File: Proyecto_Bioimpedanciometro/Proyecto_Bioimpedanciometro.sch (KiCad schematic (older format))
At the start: 29 parts, among them IC1 ATMEGA328P-A, P1 CONN_01X10, P2 CONN_01X04, U1 ADG849, U2 AD8606, U3 APD3339, Y1 Crystal_Small

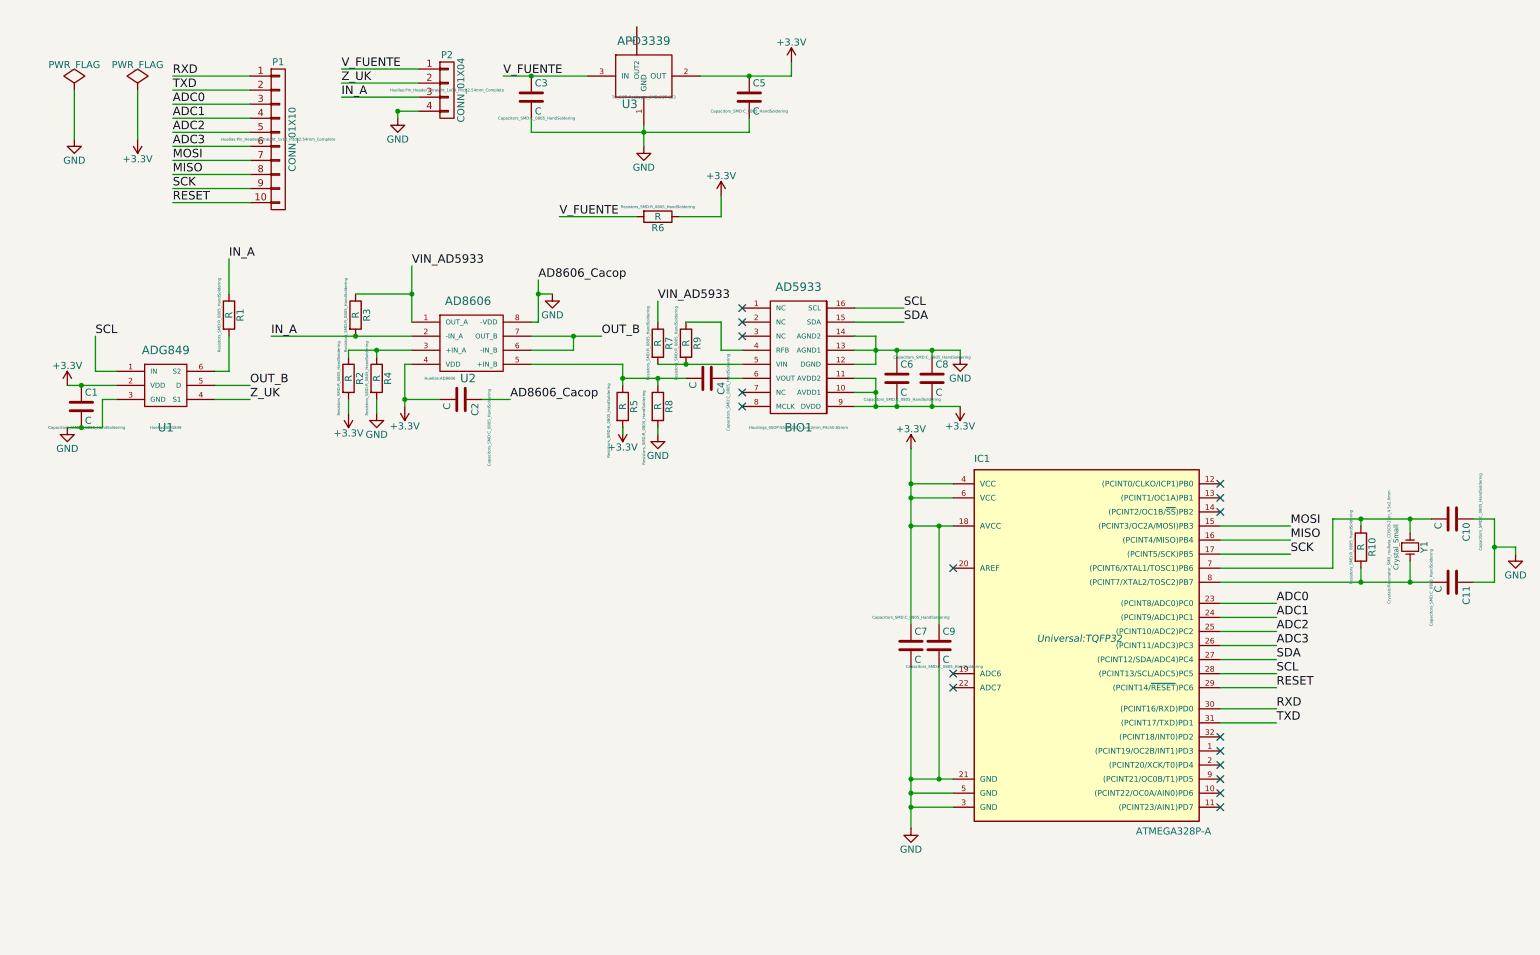
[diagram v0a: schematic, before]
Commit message: Segunda Version
Empieza PCB
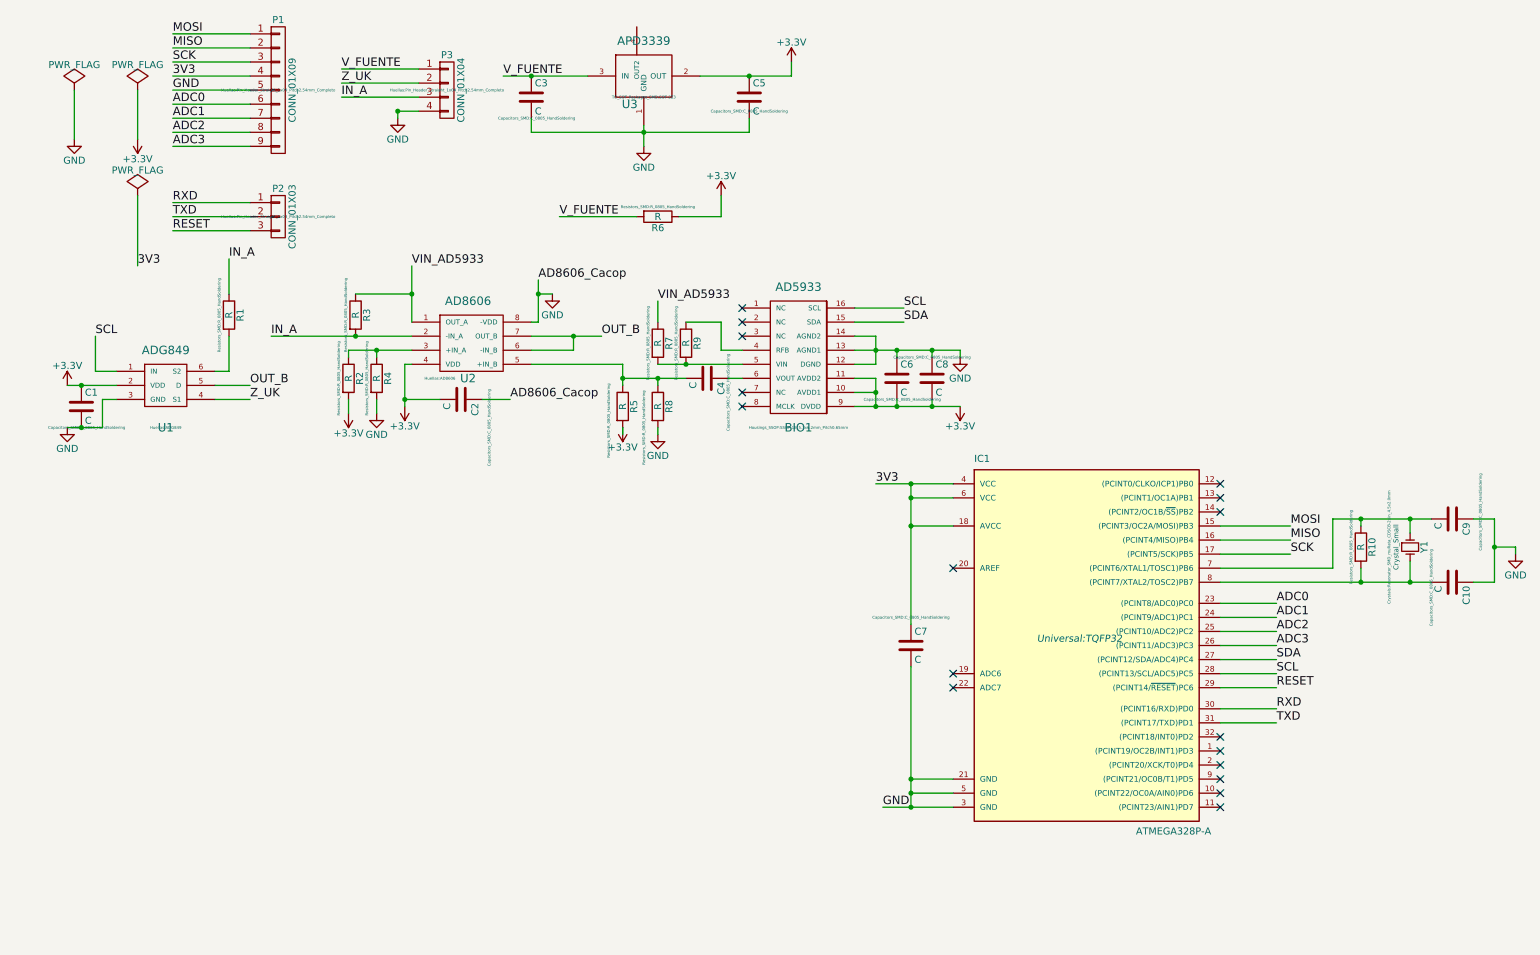
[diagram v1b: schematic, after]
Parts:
- removed C9: C, Capacitors_SMD:C_0805_HandSoldering, symbol C
- removed P1: CONN_01X10, Huellas:Pin_Header_Straight_1x10_Pitch2.54mm_Completo, symbol CONN_01X10
- added P1: CONN_01X09, Huellas:Pin_Header_Straight_1x09_Pitch2.54mm_Completo, symbol CONN_01X09
- added P2: CONN_01X03, Huellas:Pin_Header_Straight_1x03_Pitch2.54mm_Completo, symbol CONN_01X03
- renumbered C11 to C10, C10 to C9, P2 to P3
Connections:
- net +3V3: no longer C7.1, IC1.18 (AVCC), IC1.4 (VCC), IC1.6 (VCC)
- net ADC0: now also P1.6 (P6)
- net ADC1: now also P1.7 (P7)
- net ADC2: now also P1.8 (P8)
- net ADC3: now also P1.9 (P9)
- net GND: now also P1.5 (P5)
- net MISO: now also P1.2 (P2)
- net MOSI: now also P1.1 (P1)
- net RESET: now also P2.3 (P3)
- net RXD: now also P2.1 (P1)
- net SCK: now also P1.3 (P3)
- net TXD: now also P2.2 (P2)
- new net 3V3: C7.1, IC1.18 (AVCC), IC1.4 (VCC), IC1.6 (VCC), P1.4 (P4)
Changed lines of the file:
@@
 	-1   0    0    1
-$EndComp
-$Comp
-L +3.3V #PWR09
-U 1 1 5906C3D4
-P 6850 3600
-F 0 "#PWR09" H 6850 3450 50  0001 C CNN
-F 1 "+3.3V" H 6850 3740 50  0000 C CNN
-F 2 "" H 6850 3600 50  0000 C CNN
-F 3 "" H 6850 3600 50  0000 C CNN
-	1    6850 3600
-	1    0    0    -1
-$EndComp
-$Comp
-L GND #PWR010
-U 1 1 5906C412
-P 6850 6300
-F 0 "#PWR010" H 6850 6050 50  0001 C CNN
-F 1 "GND" H 6850 6150 50  0000 C CNN
-F 2 "" H 6850 6300 50  0000 C CNN
-F 3 "" H 6850 6300 50  0000 C CNN
-	1    6850 6300
-	1    0    0    -1
 $EndComp
 Text Label 2150 3150 0    60   ~ 0
@@
 NoConn ~ 7150 4450
 $Comp
-L GND #PWR011
+L GND #PWR09
 U 1 1 5908C4BA
 P 4950 1450
-F 0 "#PWR011" H 4950 1200 50  0001 C CNN
+F 0 "#PWR09" H 4950 1200 50  0001 C CNN
 F 1 "GND" H 4950 1300 50  0000 C CNN
 F 2 "" H 4950 1450 50  0000 C CNN
@@
 $EndComp
 $Comp
-L +3.3V #PWR012
+L +3.3V #PWR010
 U 1 1 5908C540
 P 6000 850
-F 0 "#PWR012" H 6000 700 50  0001 C CNN
+F 0 "#PWR010" H 6000 700 50  0001 C CNN
 F 1 "+3.3V" H 6000 990 50  0000 C CNN
 F 2 "" H 6000 850 50  0000 C CNN
@@
 $EndComp
 $Comp
-L GND #PWR013
+L GND #PWR011
 U 1 1 59090FFD
 P 4300 2500
-F 0 "#PWR013" H 4300 2250 50  0001 C CNN
+F 0 "#PWR011" H 4300 2250 50  0001 C CNN
 F 1 "GND" H 4300 2350 50  0000 C CNN
 F 2 "" H 4300 2500 50  0000 C CNN
@@
 $EndComp
 $Comp
-L +3.3V #PWR014
+L +3.3V #PWR012
 U 1 1 5909102D
 P 3250 3300
-F 0 "#PWR014" H 3250 3150 50  0001 C CNN
+F 0 "#PWR012" H 3250 3150 50  0001 C CNN
 F 1 "+3.3V" H 3250 3440 50  0000 C CNN
 F 2 "" H 3250 3300 50  0000 C CNN
@@
 Z_UK
 $Comp
-L GND #PWR015
+L GND #PWR013
 U 1 1 590947E6
 P 3200 1250
-F 0 "#PWR015" H 3200 1000 50  0001 C CNN
+F 0 "#PWR013" H 3200 1000 50  0001 C CNN
 F 1 "GND" H 3200 1100 50  0000 C CNN
 F 2 "" H 3200 1250 50  0000 C CNN
@@
 $EndComp
 $Comp
-L +3.3V #PWR016
+L +3.3V #PWR014
 U 1 1 5909785B
 P 5500 1800
-F 0 "#PWR016" H 5500 1650 50  0001 C CNN
+F 0 "#PWR014" H 5500 1650 50  0001 C CNN
 F 1 "+3.3V" H 5500 1940 50  0000 C CNN
 F 2 "" H 5500 1800 50  0000 C CNN
@@
 IN_A
 $Comp
-L PWR_FLAG #FLG017
+L PWR_FLAG #FLG015
 U 1 1 590A29EE
 P 900 1050
-F 0 "#FLG017" H 900 1145 50  0001 C CNN
+F 0 "#FLG015" H 900 1145 50  0001 C CNN
 F 1 "PWR_FLAG" H 900 1230 50  0000 C CNN
 F 2 "" H 900 1050 50  0000 C CNN
@@
 $EndComp
 $Comp
-L PWR_FLAG #FLG018
+L PWR_FLAG #FLG016
 U 1 1 590A2A28
 P 1350 1050
-F 0 "#FLG018" H 1350 1145 50  0001 C CNN
+F 0 "#FLG016" H 1350 1145 50  0001 C CNN
 F 1 "PWR_FLAG" H 1350 1230 50  0000 C CNN
 F 2 "" H 1350 1050 50  0000 C CNN
@@
 $EndComp
 $Comp
-L GND #PWR019
+L GND #PWR017
 U 1 1 590A2B52
 P 900 1400
-F 0 "#PWR019" H 900 1150 50  0001 C CNN
+F 0 "#PWR017" H 900 1150 50  0001 C CNN
 F 1 "GND" H 900 1250 50  0000 C CNN
 F 2 "" H 900 1400 50  0000 C CNN
@@
 $EndComp
 $Comp
-L +3.3V #PWR020
+L +3.3V #PWR018
 U 1 1 590A2B8C
 P 1350 1400
-F 0 "#PWR020" H 1350 1250 50  0001 C CNN
+F 0 "#PWR018" H 1350 1250 50  0001 C CNN
 F 1 "+3.3V" H 1350 1540 50  0000 C CNN
 F 2 "" H 1350 1400 50  0000 C CNN
@@
 $EndComp
 $Comp
-L C C10
+L C C9
 U 1 1 590BC56B
 P 10700 4100
-F 0 "C10" H 10725 4200 50  0000 L CNN
+F 0 "C9" H 10725 4200 50  0000 L CNN
 F 1 "C" H 10725 4000 50  0000 L CNN
 F 2 "Capacitors_SMD:C_0805_HandSoldering" H 10650 4300 20  0000 C CNN
@@
 $EndComp
 $Comp
-L C C11
+L C C10
 U 1 1 590BC5EC
 P 10700 4550
-F 0 "C11" H 10725 4650 50  0000 L CNN
+F 0 "C10" H 10725 4650 50  0000 L CNN
 F 1 "C" H 10725 4450 50  0000 L CNN
 F 2 "Capacitors_SMD:C_0805_HandSoldering" H 10738 4400 20  0000 C CNN
@@
 $EndComp
 $Comp
-L GND #PWR021
+L GND #PWR019
 U 1 1 590BD420
 P 11150 4350
-F 0 "#PWR021" H 11150 4100 50  0001 C CNN
+F 0 "#PWR019" H 11150 4100 50  0001 C CNN
 F 1 "GND" H 11150 4200 50  0000 C CNN
 F 2 "" H 11150 4350 50  0000 C CNN
@@
 	1    0    0    -1
 $EndComp
-$Comp
-L C C9
-U 1 1 590CC03D
-P 7050 5000
-F 0 "C9" H 7075 5100 50  0000 L CNN
-F 1 "C" H 7075 4900 50  0000 L CNN
-F 2 "Capacitors_SMD:C_0805_HandSoldering" H 7088 4850 20  0000 C CNN
-F 3 "" H 7050 5000 50  0000 C CNN
-	1    7050 5000
-	1    0    0    -1
-$EndComp
 Wire Wire Line
 	4800 3000 4800 3150
@@
 	9050 5200 9450 5200
 Wire Wire Line
-	6850 3600 6850 4850
-Wire Wire Line
-	6850 4150 7150 4150
-Connection ~ 6850 3850
-Wire Wire Line
-	6850 6150 7150 6150
-Wire Wire Line
-	6850 5150 6850 6300
+	6650 6150 7150 6150
 Wire Wire Line
 	6850 6050 7150 6050
@@
 	9050 4700 9450 4700
 Wire Wire Line
+	2150 850  1600 850
+Wire Wire Line
 	2150 1150 1600 1150
 Wire Wire Line
@@
 Wire Wire Line
 	2150 1350 1600 1350
-Wire Wire Line
-	2150 1450 1600 1450
 Wire Wire Line
 	9050 4550 10550 4550
@@
 	11150 4300 11150 4350
 Connection ~ 11000 4300
-Connection ~ 6850 3950
 Wire Wire Line
 	6850 5950 7150 5950
@@
 	7000 2950 7000 2900
 Connection ~ 7000 2900
-Wire Wire Line
-	7150 3950 6850 3950
-Wire Wire Line
-	7150 3850 6850 3850
 Connection ~ 6850 6050
-Connection ~ 6850 6150
-Connection ~ 6850 4150
-Wire Wire Line
-	7050 4850 7050 4150
-Connection ~ 7050 4150
-Wire Wire Line
-	7050 5150 7050 5950
-Connection ~ 7050 5950
 Connection ~ 6850 5950
 $Comp
@@
 TXD
 Wire Wire Line
-	2150 950  1600 950
-Wire Wire Line
-	2150 1050 1600 1050
-Text Label 1600 950  0    60   ~ 0
+	2150 650  1600 650
+Wire Wire Line
+	2150 750  1600 750
+Text Label 1600 1850 0    60   ~ 0
 RXD
-Text Label 1600 1050 0    60   ~ 0
+Text Label 1600 1950 0    60   ~ 0
 TXD
 Wire Wire Line
@@
 MOSI
 Wire Wire Line
-	10550 4100 9850 4100
-Wire Wire Line
-	9850 4100 9850 4450
+	9850 4100 10550 4100
+Wire Wire Line
+	9850 4450 9850 4100
 Text Label 9550 4250 0    60   ~ 0
 MISO
@@
 SCK
 $Comp
-L CONN_01X04 P2
+L CONN_01X04 P3
 U 1 1 590DFDA3
 P 3550 1050
-F 0 "P2" H 3550 1300 50  0000 C CNN
+F 0 "P3" H 3550 1300 50  0000 C CNN
 F 1 "CONN_01X04" V 3650 1050 50  0000 C CNN
 F 2 "Huellas:Pin_Header_Straight_1x04_Pitch2.54mm_Completo" H 3550 1050 20  0000 C CNN
@@
 $EndComp
 Wire Wire Line
-	2150 1550 1600 1550
-Wire Wire Line
-	2150 1650 1600 1650
-Text Label 1600 1550 0    60   ~ 0
+	2150 1450 1600 1450
+Wire Wire Line
+	2150 1850 1600 1850
+Text Label 1600 650  0    60   ~ 0
 MOSI
-Text Label 1600 1650 0    60   ~ 0
+Text Label 1600 750  0    60   ~ 0
 MISO
 Wire Wire Line
-	2150 1750 1600 1750
-Text Label 1600 1750 0    60   ~ 0
+	2150 1950 1600 1950
+Text Label 1600 850  0    60   ~ 0
 SCK
 Wire Wire Line
-	2150 1850 1600 1850
-$Comp
-L CONN_01X10 P1
-U 1 1 590E2BF1
-P 2350 1400
-F 0 "P1" H 2350 1950 50  0000 C CNN
-F 1 "CONN_01X10" V 2450 1400 50  0000 C CNN
-F 2 "Huellas:Pin_Header_Straight_1x10_Pitch2.54mm_Completo" H 2350 1400 20  0000 C CNN
-F 3 "" H 2350 1400 50  0000 C CNN
-	1    2350 1400
-	1    0    0    -1
-$EndComp
-Text Label 1600 1850 0    60   ~ 0
+	2150 2050 1600 2050
+Text Label 1600 2050 0    60   ~ 0
 RESET
 $Comp
@@
 Connection ~ 950  3450
 Connection ~ 950  3150
+$Comp
+L CONN_01X03 P2
+U 1 1 590D1EDC
+P 2350 1950
+F 0 "P2" H 2350 2150 50  0000 C CNN
+F 1 "CONN_01X03" V 2450 1950 50  0000 C CNN
+F 2 "Huellas:Pin_Header_Straight_1x03_Pitch2.54mm_Completo" H 2350 1950 20  0000 C CNN
+F 3 "" H 2350 1950 50  0000 C CNN
+	1    2350 1950
+	1    0    0    -1
+$EndComp
+$Comp
+L CONN_01X09 P1
+U 1 1 590D59C9
+P 2350 1050
+F 0 "P1" H 2350 1550 50  0000 C CNN
+F 1 "CONN_01X09" V 2450 1050 50  0000 C CNN
+F 2 "Huellas:Pin_Header_Straight_1x09_Pitch2.54mm_Completo" H 2350 1050 20  0000 C CNN
+F 3 "" H 2350 1050 50  0000 C CNN
+	1    2350 1050
+	1    0    0    -1
+$EndComp
+Wire Wire Line
+	2150 950  1600 950
+Wire Wire Line
+	2150 1050 1600 1050
+Text Label 1600 1050 0    60   ~ 0
+GND
+Text Label 1600 950  0    60   ~ 0
+3V3
+Wire Wire Line
+	6850 5150 6850 6150
+Connection ~ 6850 6150
+Text Label 6600 3850 0    60   ~ 0
+3V3
+Text Label 6650 6150 0    60   ~ 0
+GND
+Wire Wire Line
+	6600 3850 7150 3850
+Connection ~ 6850 3850
+Wire Wire Line
+	6850 3950 7150 3950
+Connection ~ 6850 3950
+Wire Wire Line
+	6850 4150 7150 4150
+Connection ~ 6850 4150
+$Comp
+L PWR_FLAG #FLG020
+U 1 1 590E8654
+P 1350 1800
+F 0 "#FLG020" H 1350 1895 50  0001 C CNN
+F 1 "PWR_FLAG" H 1350 1980 50  0000 C CNN
+F 2 "" H 1350 1800 50  0000 C CNN
+F 3 "" H 1350 1800 50  0000 C CNN
+	1    1350 1800
+	1    0    0    -1
+$EndComp
+Wire Wire Line
+	1350 1800 1350 2300
+Text Label 1350 2300 0    60   ~ 0
+3V3
+Wire Wire Line
+	6850 3850 6850 4850
 $EndSCHEMATC

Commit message: Tercera Version
Revisar conexion bajo el micro, se hizo teniendo en cuenta simetria
segun lo hablado.
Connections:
- net RXD: now also P2.2 (P2); no longer P2.1 (P1)
- net TXD: now also P2.1 (P1); no longer P2.2 (P2)
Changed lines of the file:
@@
 Wire Wire Line
 	2150 750  1600 750
+Text Label 1600 1950 0    60   ~ 0
+RXD
 Text Label 1600 1850 0    60   ~ 0
-RXD
-Text Label 1600 1950 0    60   ~ 0
 TXD
 Wire Wire Line
@@
 	2150 1450 1600 1450
 Wire Wire Line
-	2150 1850 1600 1850
+	2150 1950 1600 1950
 Text Label 1600 650  0    60   ~ 0
 MOSI
@@
 MISO
 Wire Wire Line
-	2150 1950 1600 1950
+	2150 1850 1600 1850
 Text Label 1600 850  0    60   ~ 0
 SCK
